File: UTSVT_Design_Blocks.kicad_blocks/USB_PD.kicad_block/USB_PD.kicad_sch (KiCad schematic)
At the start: 30 parts, among them Q1 SI7997DP-T1-GE3, Q2 SI7997DP-T1-GE3, U1 CYPD3177-24LQ

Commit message: lowk forgot to push the right thing
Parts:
- removed D1: TPD2EUSB30DRTR, Components:TPD2EUSB30DRTR, symbol TPD2EUSB30:TPD2EUSB30DRTR
- removed D2: SMBJ24A-E3_52, Components:DIOM5436X244N, symbol SMBJ24A:SMBJ24A-E3_52
- removed D3, D4: SMBJ10A-E3_52, Components:DIOM5436X244N, symbol SMBJ10A:SMBJ10A-E3_52
- removed R12: 4.7k, Resistor_SMD:R_0603_1608Metric_Pad0.98x0.95mm_HandSolder, symbol Device:R_Small
- removed U1: CYPD3177-24LQ, Components:CYPD3177-24LQXQ, symbol Interface_USB:CYPD3177-24LQ
- added D1: TPD2EUSB30DRTR, SOTFL35P100X50-3N, symbol USB_PD_Symbols:TPD2EUSB30DRTR
- added D2, D6: SMBJ10A-E3_52, DIOM5436X244N, symbol USB_PD_Symbols:SMBJ10A-E3_52
- added D5: SMBJ24A-E3_52, DIOM5436X244N, symbol USB_PD_Symbols:SMBJ24A-E3_52
- added IC1: CYPD3177-24LQXQ, QFN50P400X400X60-25N-D, symbol USB_PD_Symbols:CYPD3177-24LQXQ
- added R15: 4.7k, Resistor_SMD:R_0603_1608Metric_Pad0.98x0.95mm_HandSolder, symbol Device:R_Small
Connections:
- net CC1: now also IC1.15 (CC1)
- net CC2: now also IC1.14 (CC2)
- net D+: now also D1.1 (D+)
- net D-: now also D1.2 (D-)
- net GND: now also D1.3 (GND), D5.2 (A), IC1.19 (GND_1), IC1.22 (GND_2), IC1.25 (GND_3), IC1.6 (ISNK_FINE)
- net ISINK_COARSE: now also IC1.5 (ISNK_COARSE)
- net PD_GPIO_1: now also IC1.8 (GPIO_1)
- net PD_HPI_INT: now also IC1.7 (HPI_INT)
- net SAFE_PWR_EN: now also IC1.4 (SAFE_PWR_EN)
- net SCL: now also IC1.13 (HPI_SCL)
- net SDA: now also IC1.12 (HPI_SDA)
- net VBUS_FET_EN: now also IC1.3 (VBUS_FET_EN)
- net VBUS_IN: now also D5.1 (K), IC1.18 (VBUS_IN)
- net VBUS_MIN: now also IC1.1 (VBUS_MIN)
- net VBUS_OUT: now also IC1.11 (VDC_OUT)
- net VDDD: now also IC1.2 (VBUS_MAX), IC1.23 (VDDD), R15.1
- net at C3.2, C5.2, Q2.2 (G1)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: now also D6.2 (A)
- net at C2.2, C4.2, Q1.2 (G1)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: now also D2.2 (A)
- net at Q1.1 (S1), Q1.3 (S2), R11.2: now also D2.1 (K)
- net at C6.2: now also IC1.24 (VCCD)
- net at Q2.1 (S1), Q2.3 (S2): now also D6.1 (K)
- new net: IC1.10 (FLIP), R15.2
- new net PD_FAULT: IC1.9 (FAULT)
- no-connect marks 1 -> 4
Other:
- note added: "Active low HPI interrupt pin"
- note added: "GPIO for HPI interface"
- note added: "High if fault, low otherwise"
- moved on the sheet: C6, C7, C8, C9, R13, R14

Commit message: lcsc
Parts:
- C1: LCSC P/N (none) -> C440198
- C2, C3, C4, C5, C6, C7: LCSC P/N (none) -> C15849; P/N (none) -> MLASU168SB5105KTNA01
- C8, C9: LCSC P/N (none) -> C14663; P/N (none) -> MLASH168SB7104KTNA01
- D1: footprint SOTFL35P100X50-3N -> Components:TPD2EUSB30DRTR
- D2, D5, D6: footprint DIOM5436X244N -> Components:DIOM5436X244N
- IC1: footprint QFN50P400X400X60-25N-D -> Components:CYPD3177-24LQXQ
- Q1, Q2: footprint SI7288DPT1GE3 -> Components:SI7288DPT1GE3
- R1, R2: LCSC P/N (none) -> C23186
- R10, R7, R8: LCSC P/N (none) -> C23186; P/N (none) -> CRCW06035K10FKEC
- R11, R6: LCSC P/N (none) -> C4117233; P/N (none) -> CRCW060349K9FKEC
- R13, R14: LCSC P/N (none) -> C844925; P/N (none) -> CRCW06032K20FKEA
- R15: LCSC P/N (none) -> C23162; P/N (none) -> CRCW06034K70FKEA
- R3, R4, R9: LCSC P/N (none) -> C21190; P/N (none) -> CRCW06031K00FKEI
- R5: LCSC P/N (none) -> C25804; P/N (none) -> CRCW060310K0FKEI

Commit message: footprints
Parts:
- D1: footprint Components:TPD2EUSB30DRTR -> UTSVT_ICs:TPD2EUSB30DRTR
- D2, D5, D6: footprint Components:DIOM5436X244N -> Diode_SMD:D_SMB
- IC1: footprint Components:CYPD3177-24LQXQ -> UTSVT_ICs:CYPD3177-24LQXQ
- Q1, Q2: footprint Components:SI7288DPT1GE3 -> UTSVT_ICs:SI7997DP-T1-GE3
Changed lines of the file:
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@@
 			)
 		)
-		(property "Footprint" "Components:DIOM5436X244N"
+		(property "Footprint" "Diode_SMD:D_SMB"
 			(at 1.6 149.86 0)
 			(effects
@@
 			)
 		)
-		(property "Footprint" "Components:CYPD3177-24LQXQ"
+		(property "Footprint" "UTSVT_ICs:CYPD3177-24LQXQ"
 			(at 168.91 155.88 0)
 			(effects
@@
 			)
 		)
-		(property "Footprint" "Components:SI7288DPT1GE3"
+		(property "Footprint" "UTSVT_ICs:SI7997DP-T1-GE3"
 			(at 86.36 233.35 0)
 			(effects
@@
 			)
 		)
-		(property "Footprint" "Components:SI7288DPT1GE3"
+		(property "Footprint" "UTSVT_ICs:SI7997DP-T1-GE3"
 			(at 96.52 266.37 0)
 			(effects
@@
 			)
 		)
-		(property "Footprint" "Components:DIOM5436X244N"
+		(property "Footprint" "Diode_SMD:D_SMB"
 			(at -2.21 182.88 0)
 			(effects
@@
 			)
 		)
-		(property "Footprint" "Components:TPD2EUSB30DRTR"
+		(property "Footprint" "UTSVT_ICs:TPD2EUSB30DRTR"
 			(at 44.45 199.06 0)
 			(effects
@@
 			)
 		)
-		(property "Footprint" "Components:SI7288DPT1GE3"
+		(property "Footprint" "UTSVT_ICs:SI7997DP-T1-GE3"
 			(at 86.36 266.37 0)
 			(effects
@@
 			)
 		)
-		(property "Footprint" "Components:SI7288DPT1GE3"
+		(property "Footprint" "UTSVT_ICs:SI7997DP-T1-GE3"
 			(at 96.52 233.35 0)
 			(effects
@@
 			)
 		)
-		(property "Footprint" "Components:DIOM5436X244N"
+		(property "Footprint" "Diode_SMD:D_SMB"
 			(at -65.71 52.07 0)
 			(effects

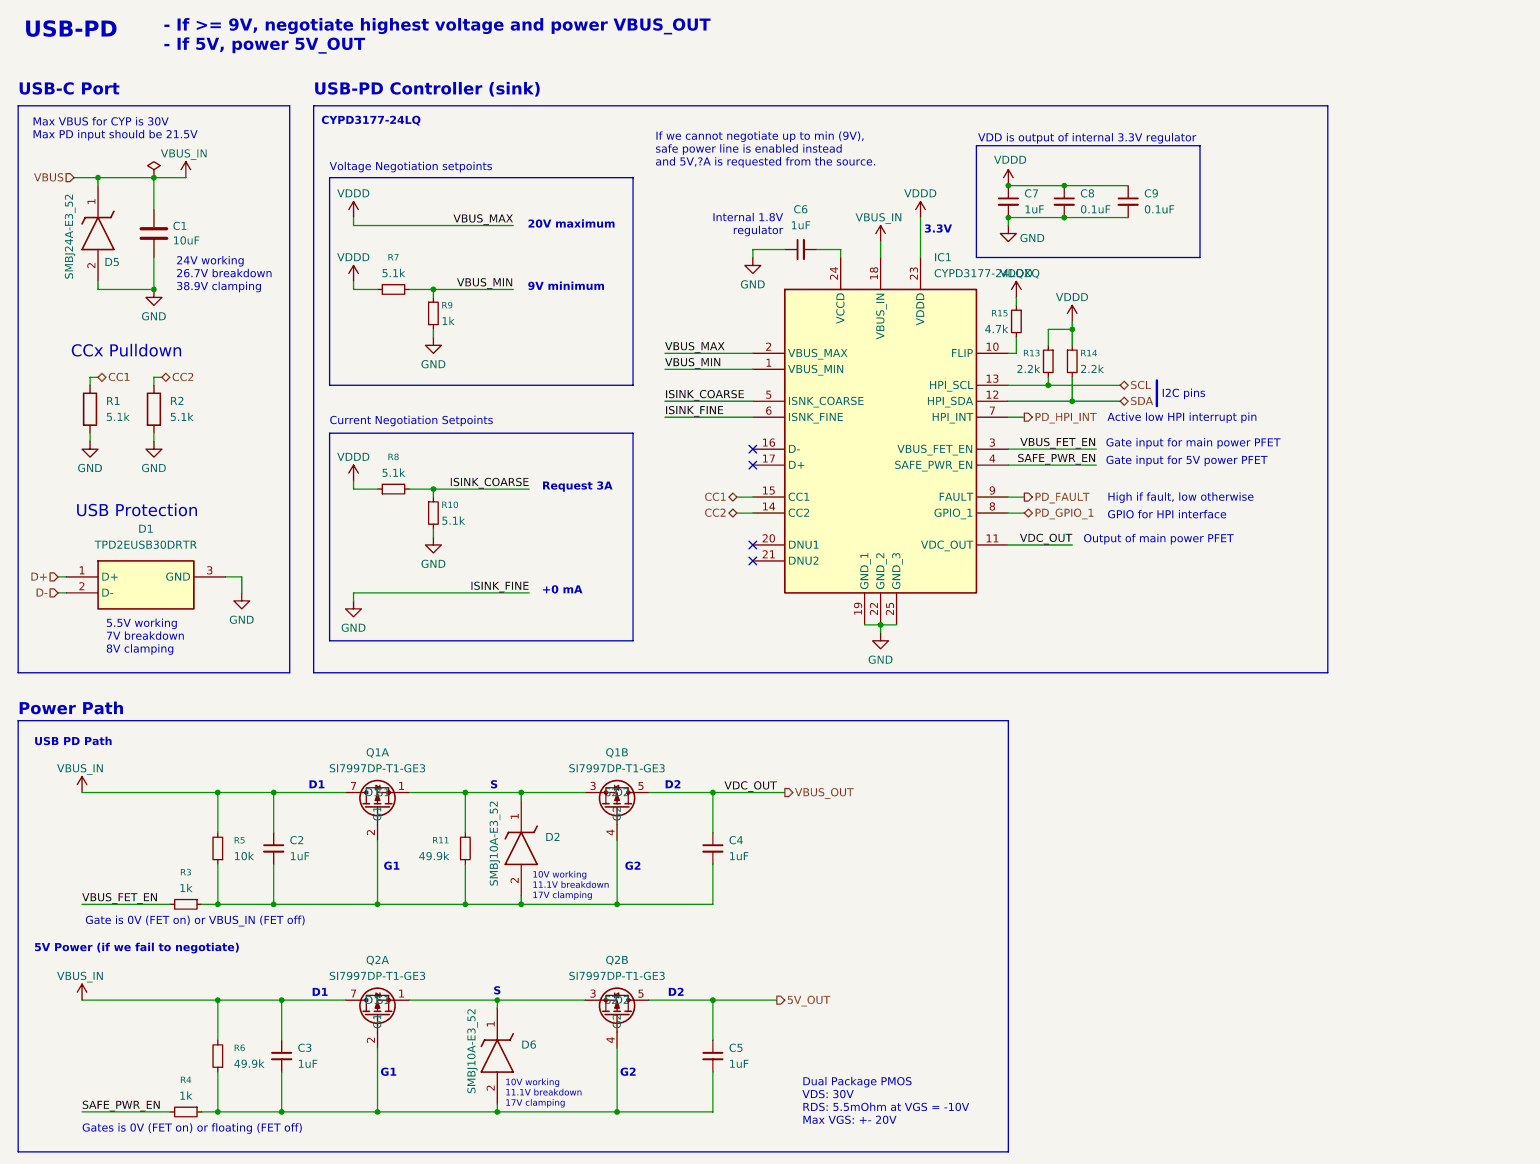
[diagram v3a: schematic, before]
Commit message: better naming so labels don't conflict
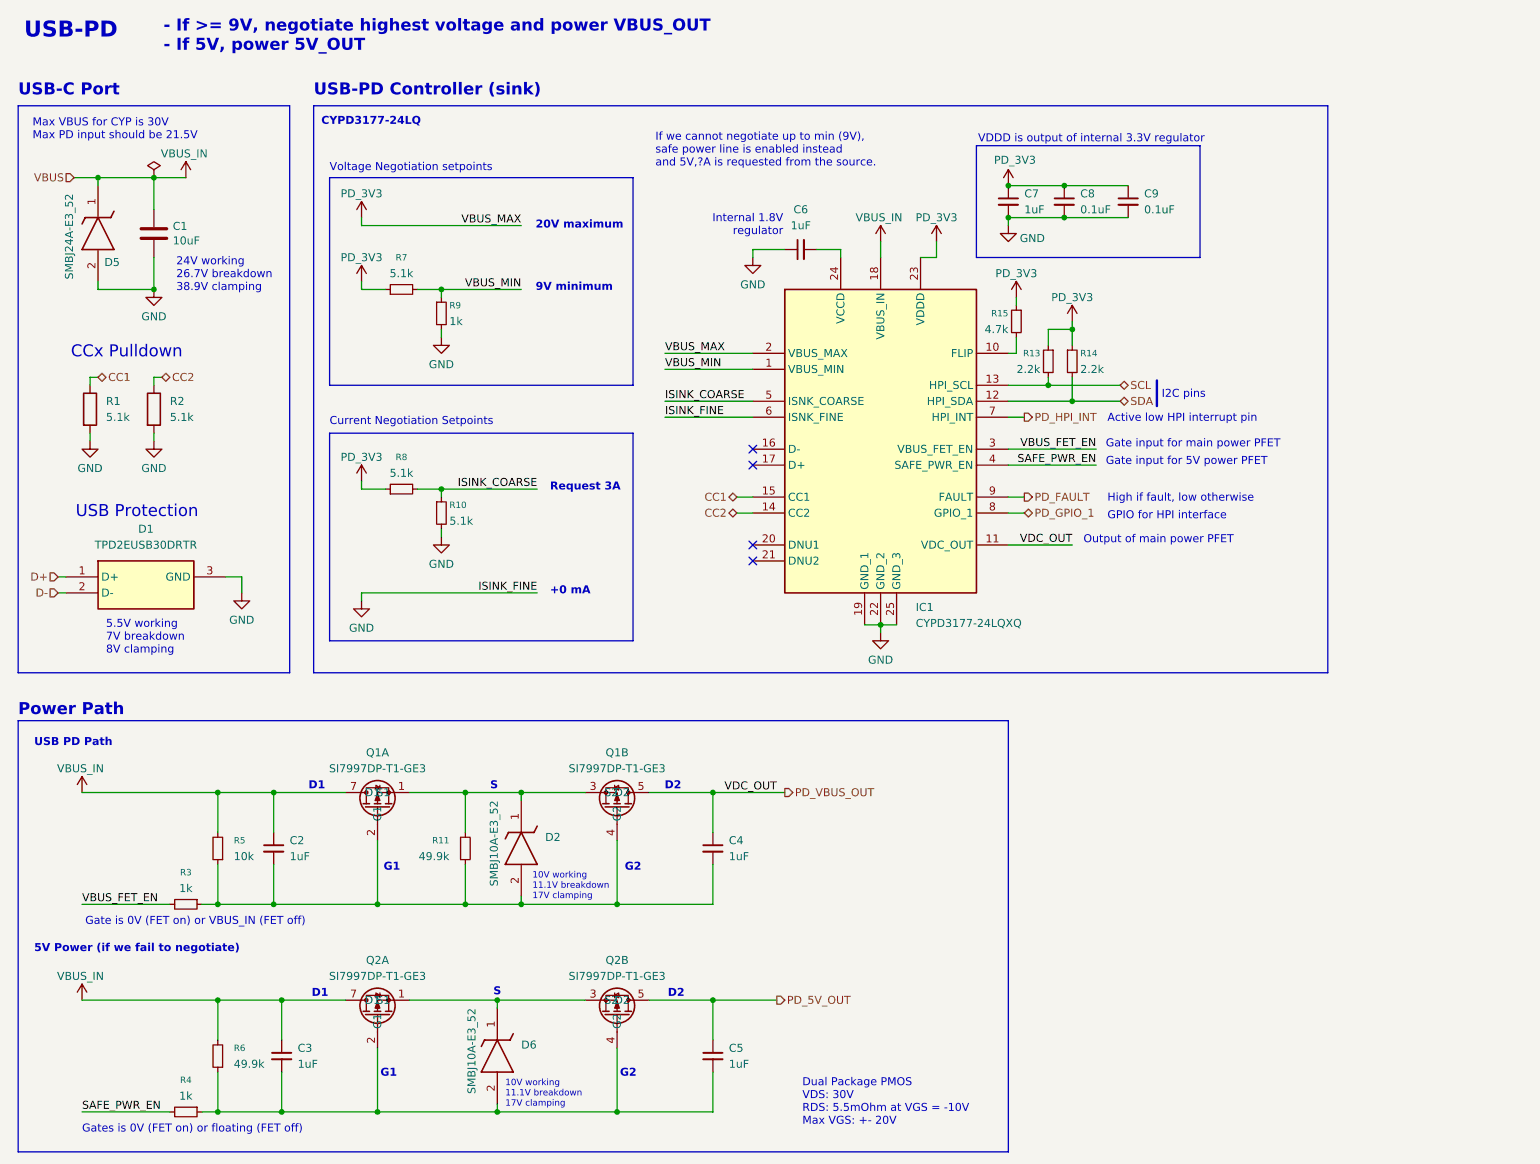
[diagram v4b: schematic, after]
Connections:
- net 5V_OUT renamed PD_5V_OUT
- net VBUS_OUT renamed PD_VBUS_OUT
- net VDDD renamed PD_3V3
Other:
- note added: "VDDD is output of internal 3.3V regulator"
- note removed: "3.3V"
- note removed: "VDD is output of internal 3.3V regulator"
- moved on the sheet: R10, R7, R8, R9
